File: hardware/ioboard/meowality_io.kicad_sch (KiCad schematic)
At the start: 4 parts

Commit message: Add USB hub and UART ICs
Signed-off-by: gatecat <gatecat@ds0.me>
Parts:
- added C? (x5): 1µ, symbol Device:C_Small
- added C? (x2): 12p, symbol Device:C_Small
- added C? (x3): 10µ, symbol Device:C_Small
- added J? (x2): Conn_01x03, symbol Connector_Generic:Conn_01x03
- added J?: Conn_01x05, symbol Connector_Generic:Conn_01x05
- added R? (x2): 2.2k, symbol Device:R_Small
- added R?: 2.7k, symbol Device:R_Small
- added R? (x4): 1k, symbol Device:R_Small
- added U? (x3): CH330N, Package_SO:SOIC-8_3.9x4.9mm_P1.27mm, symbol Interface_USB:CH330N
- added U?: FE1.1s, Package_SO:SSOP-28_3.9x9.9mm_P0.635mm, symbol Interface_USB:FE1.1s
- added U?: 24LC00, symbol Memory_EEPROM:24LC00
- added Y?: 12MHz, symbol Device:Crystal_GND24
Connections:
- net +3V3: now also U?.3 (VDD), U?.4 (VDD), C?.1, C?.1, C?.1, U?.5 (VCC), U?.5 (VCC), U?.8 (V3), U?.8 (V3)
- net +5V: now also U?.12 (VCONN), U?.13 (VCONN), C?.1, R?.2, U?.20 (VDD5)
- net GND: now also C?.1, C?.1, C?.2, C?.2, C?.2, C?.2, C?.2, C?.2, C?.2, C?.2, J?.3 (Pin_3), J?.3 (Pin_3), J?.5 (Pin_5), R?.1, R?.2, U?.1 (A0), U?.1 (VSS), U?.2 (A1), U?.3 (A2), U?.3 (GND), U?.3 (GND), U?.4 (GND), Y?.2, Y?.4
- net LEFT_UART_RX: now also J?.1 (Pin_1), U?.6 (TXD)
- net LEFT_UART_TX: now also J?.2 (Pin_2), U?.7 (RXD)
- net RIGHT_UART_RX: now also J?.1 (Pin_1), U?.6 (TXD)
- net RIGHT_UART_TX: now also J?.2 (Pin_2), U?.7 (RXD)
- net USB2L_D+: now also U?.7 (DP3)
- net USB2L_D-: now also U?.6 (DM3)
- net USB2R_D+: now also U?.5 (DP4)
- net USB2R_D-: now also U?.4 (DM4)
- net USB2_D+: now also U?.16 (DPU)
- net USB2_D-: now also U?.15 (DMU)
- net VBUS: now also U?.2 (VBUS)
- new net: R?.1, U?.14 (REXT)
- new net: R?.1, U?.18 (VBUSM)
- new net: R?.2, U?.19 (BUSJ)
- new net: C?.2, U?.2 (XOUT), Y?.1
- new net: R?.2, U?.26 (OVCJ)
- new net: C?.2, U?.3 (XIN), Y?.3
- new net HUB_1V8: C?.1, C?.1, U?.12 (VD18_O)
- new net HUB_3V3: C?.1, C?.1, J?.1 (Pin_1), R?.1, R?.1, R?.2, R?.2, U?.13 (VD33), U?.21 (VD33_O), U?.8 (VCC)
- new net HUB_RST: J?.4 (Pin_4), R?.2, U?.17 (~{XRSTJ})
- new net HUB_SCL: J?.3 (Pin_3), R?.1, U?.23 (LED1/EESCL), U?.6 (SCL)
- new net HUB_SDA: J?.2 (Pin_2), R?.1, U?.27 (TESTJ/EESDA), U?.5 (SDA)
- new net USBUART0_D+: U?.1 (UD+), U?.11 (DP1)
- new net USBUART0_D-: U?.10 (DM1), U?.2 (UD-)
- new net USBUART1_D+: U?.1 (UD+), U?.9 (DP2)
- new net USBUART1_D-: U?.2 (UD-), U?.8 (DM2)
- no-connect marks 3 -> 10

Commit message: Add Displayport connector
Signed-off-by: gatecat <gatecat@ds0.me>
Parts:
- removed U?: CH330N, Package_SO:SOIC-8_3.9x4.9mm_P1.27mm, symbol Interface_USB:CH330N
- added F?: 500mA, symbol Device:Polyfuse_Small
- added J?: MINI_DP_SINK, symbol meowality:MINI_DP_SINK
- added R? (x2): 10k, symbol Device:R_Small
- added U? (x2): TPD4E02B04DQA, Package_SON:USON-10_2.5x1.0mm_P0.5mm, symbol Power_Protection:TPD4E02B04DQA
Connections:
- net +3V3: now also F?.1
- net DP_AUX+: now also J?.16 (AUX+)
- net DP_AUX-: now also J?.18 (AUX-)
- net DP_IN_L0+: now also J?.12 (ML_L0+), U?.2 (IO2)
- net DP_IN_L0-: now also J?.10 (ML_L0-), U?.1 (IO1)
- net DP_IN_L1+: now also J?.17 (ML_L1+), U?.5 (IO4)
- net DP_IN_L1-: now also J?.15 (ML_L1-), U?.4 (IO3)
- net DP_IN_L2+: now also J?.11 (ML_L2+), U?.5 (IO4)
- net DP_IN_L2-: now also J?.9 (ML_L2-), U?.4 (IO3)
- net DP_IN_L3+: now also J?.5 (ML_L3+), U?.2 (IO2)
- net DP_IN_L3-: now also J?.3 (ML_L3-), U?.1 (IO1)
- net GND: now also J?.1 (GND), J?.13 (GND), J?.14 (GND), J?.19 (GND), J?.7 (GND), J?.8 (GND), J?.S, R?.2, R?.2, U?.3 (G), U?.3 (G), U?.8 (G), U?.8 (G)
- new net: F?.2, J?.20 (DP_PWR)
- new net: J?.4 (CONFIG1), R?.1
- new net: J?.6 (CONFIG2), R?.1
- new net DP_HPD: J?.2 (HPD)
- no-connect marks 10 -> 9
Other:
- moved on the sheet: C?, J?, R?, U?, Y?

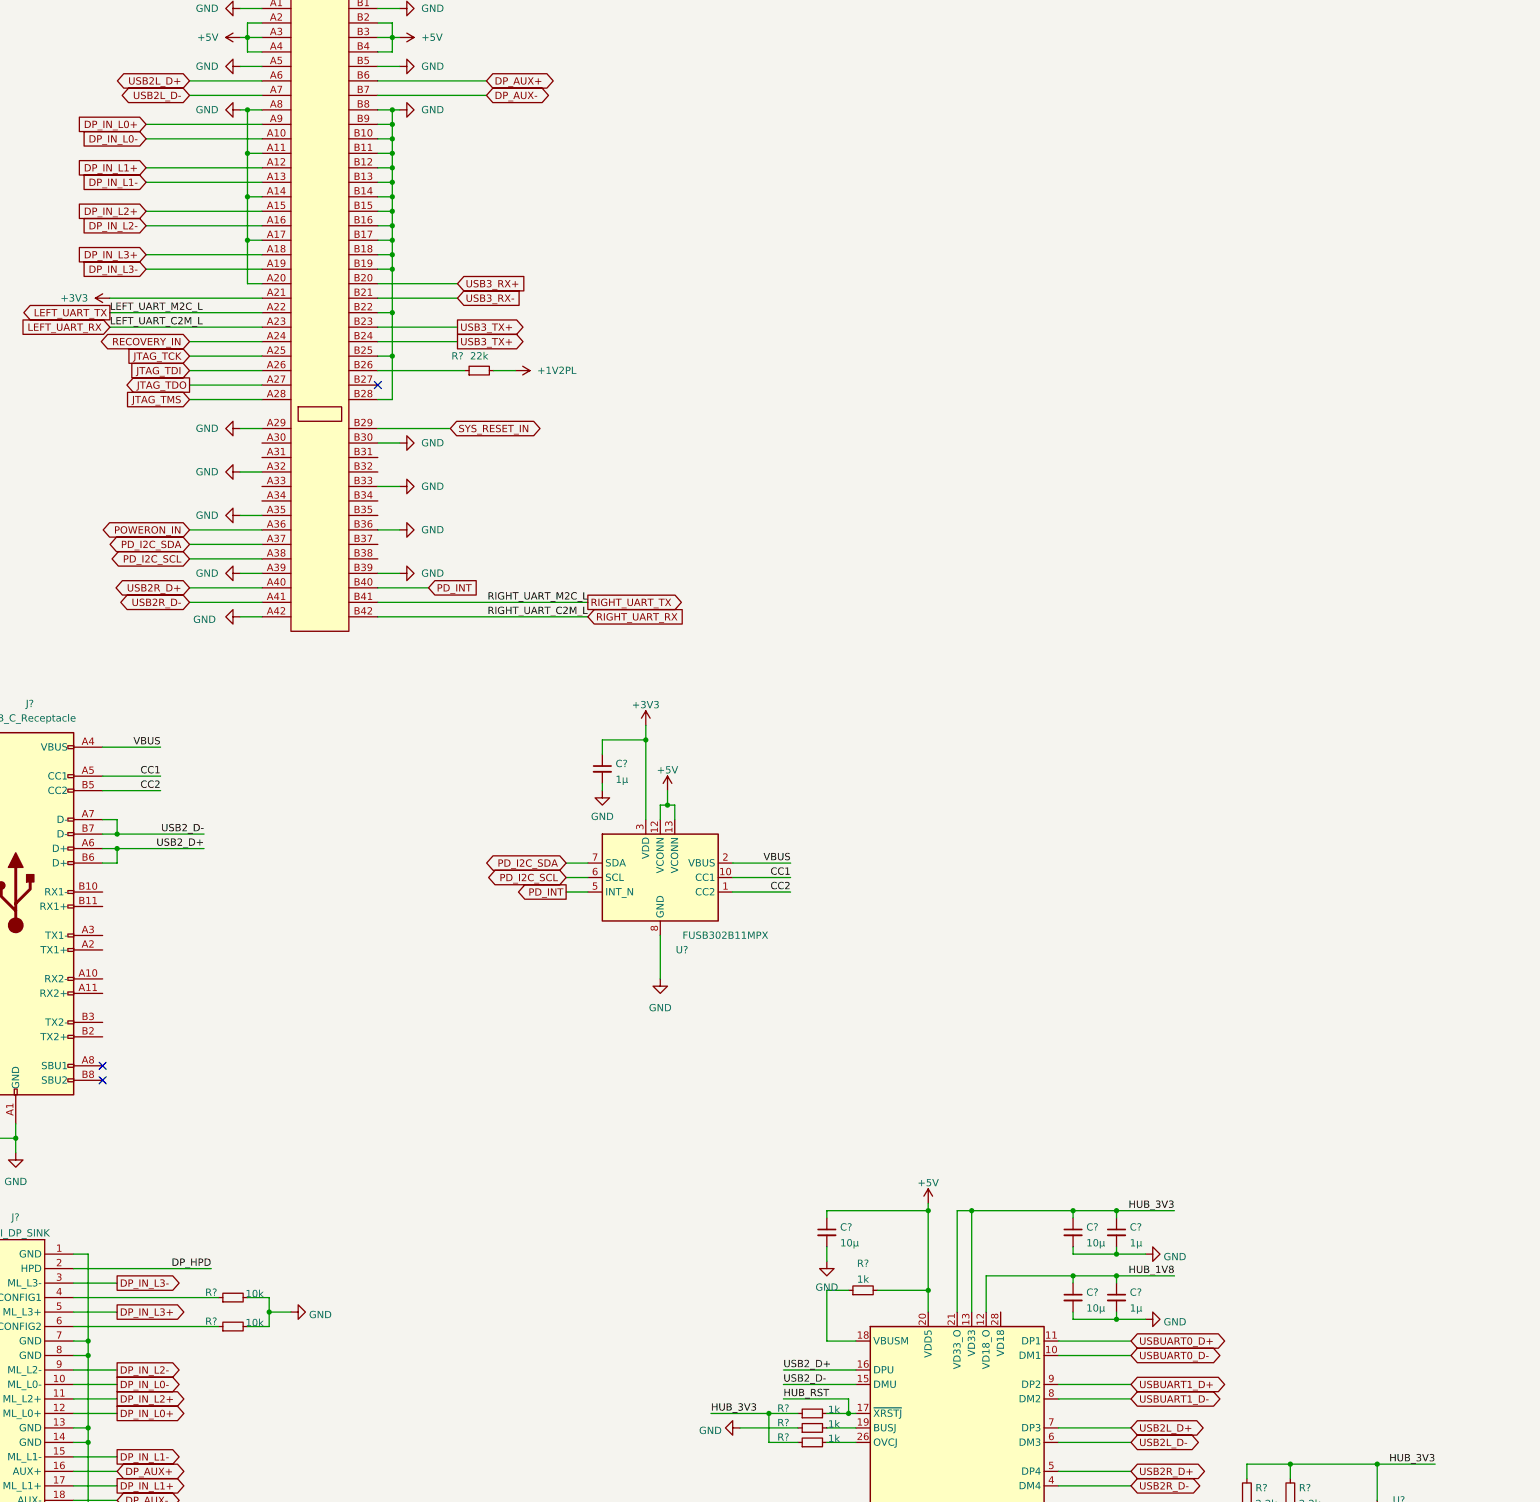
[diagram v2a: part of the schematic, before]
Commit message: Add Vbus to 5V buck
Signed-off-by: gatecat <gatecat@ds0.me>
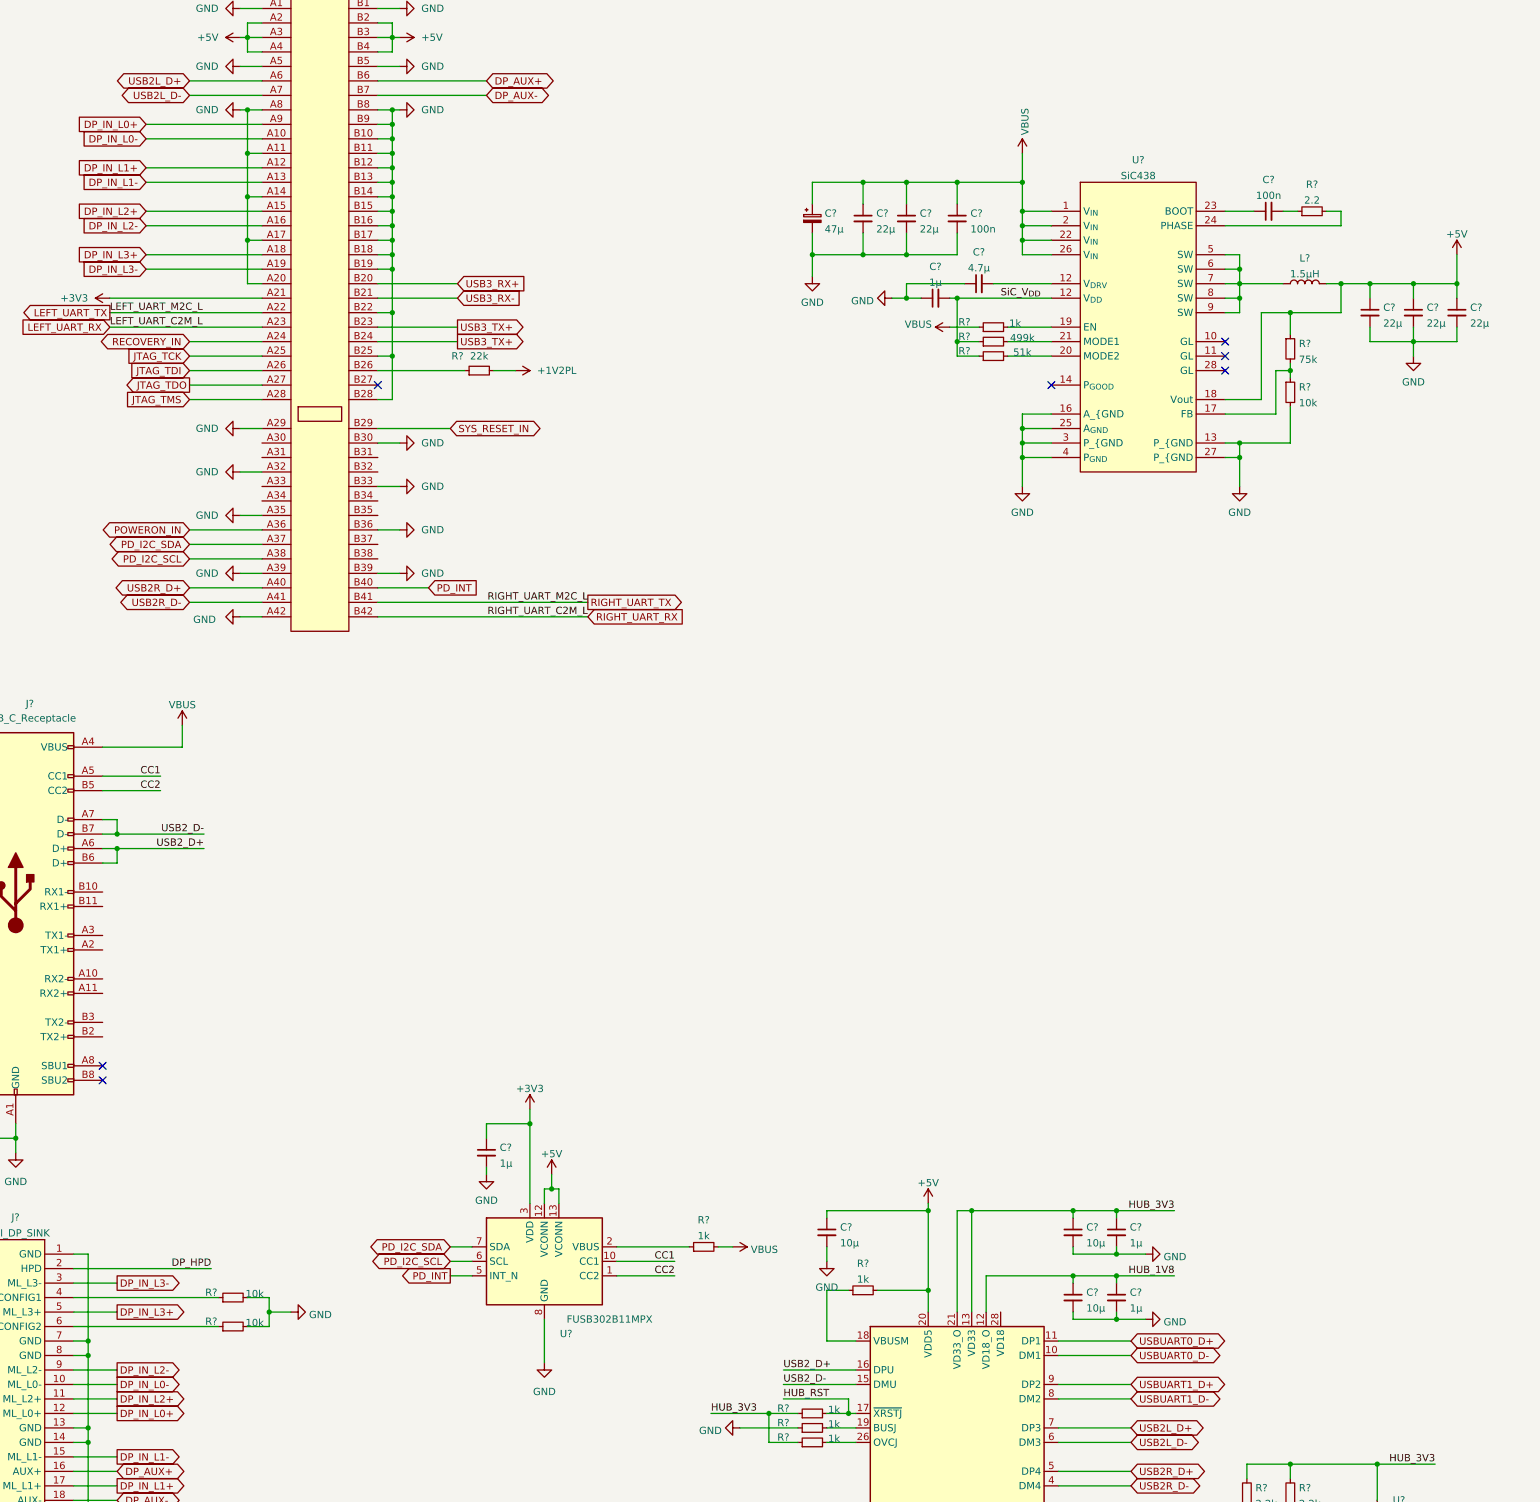
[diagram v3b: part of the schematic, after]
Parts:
- added C? (x5): 22µ, symbol Device:C_Small
- added C?: 47µ, symbol Device:CP_Small
- added C?: 1µ, symbol Device:C_Small
- added C? (x2): 100n, symbol Device:C_Small
- added C?: 4.7µ, symbol Device:C_Small
- added L?: 1.5µH, symbol Device:L
- added R?: 75k, symbol Device:R_Small
- added R?: 499k, symbol Device:R_Small
- added R?: 51k, symbol Device:R_Small
- added R? (x2): 1k, symbol Device:R_Small
- added R?: 10k, symbol Device:R_Small
- added R?: 2.2, symbol Device:R_Small
- added U?: SiC438, symbol meowality:SiC438
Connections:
- net +5V: now also C?.1, C?.1, C?.1, L?.2, R?.1, U?.18 (Vout)
- net GND: now also C?.1, C?.1, C?.2, C?.2, C?.2, C?.2, C?.2, C?.2, C?.2, R?.2, U?.13 (P_{GND), U?.16 (A_{GND), U?.25 (A_{GND}), U?.27 (P_{GND), U?.3 (P_{GND), U?.4 (P_{GND})
- net VBUS: now also C?.1, C?.1, C?.1, C?.1, R?.1, R?.2, U?.1 (V_{IN}), U?.2 (V_{IN}), U?.22 (V_{IN}), U?.26 (V_{IN}); no longer U?.2 (VBUS)
- new net: R?.1, R?.2, U?.17 (FB)
- new net: R?.2, U?.21 (MODE1)
- new net: C?.2, U?.12 (V_{DRV})
- new net: R?.2, U?.19 (EN)
- new net: R?.2, U?.20 (MODE2)
- new net: C?.1, U?.23 (BOOT)
- new net: R?.2, U?.24 (PHASE)
- new net: L?.1, U?.5 (SW), U?.6 (SW), U?.7 (SW), U?.8 (SW), U?.9 (SW)
- new net: C?.2, R?.1
- new net: R?.1, U?.2 (VBUS)
- new net SiC_V_{DD}: C?.2, R?.1, R?.1, U?.12 (V_{DRV})
- no-connect marks 9 -> 13
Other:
- moved on the sheet: C?, U?

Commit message: Add type-C mux; IO exp; 3.3V/1.8V rails
Signed-off-by: gatecat <gatecat@ds0.me>
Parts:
- added C?: 10µ, symbol Device:C_Small
- added C? (x6): 100n, symbol Device:C_Small
- added C? (x4): 1µ, symbol Device:C_Small
- added C? (x2): 22µ, symbol Device:C_Small
- added C?: 10n, symbol Device:C_Small
- added L?: 3.3µ, symbol Device:L_Small
- added R? (x5): 10k, symbol Device:R_Small
- added R? (x2): 100, symbol Device:R_Small
- added R?: 31.6k, symbol Device:R_Small
- added RN? (x2): 1k, symbol Device:R_Pack04
- added SW? (x2): SW_Push, symbol Switch:SW_Push
- added SW?: SW_SPDT, symbol Switch:SW_SPDT
- added U?: PCAL6416APW, Package_SO:TSSOP-24_4.4x7.8mm_P0.65mm, symbol Interface_Expansion:PCAL6416APW
- added U?: LD3985M18R_SOT23, Package_TO_SOT_SMD:SOT-23-5, symbol Regulator_Linear:LD3985M18R_SOT23
- added U?: HDSP-7501, Display_7Segment:HDSP-A151, symbol Display_Character:HDSP-7501
- added U?: CBTL02043A, Package_DFN_QFN:WQFN-20-1EP_2.5x4.5mm_P0.5mm_EP1x2.9mm, symbol Analog_Switch:CBTL02043A
- added U?: AP6230xWU, symbol meowality:AP6230xWU
- C? (x2): value 22µ -> 10µ
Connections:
- net +3V3: now also C?.1, C?.1, C?.1, C?.1, C?.2, L?.2, R?.1, R?.1, R?.1, U?.1 (CA), U?.1 (VDD), U?.1 (VIN), U?.10 (VDD), U?.24 (VDD_P), U?.3 (INH), U?.6 (CA), U?.6 (VDD)
- net +5V: now also C?.1, U?.1 (Vin), U?.5 (EN)
- net DP_HPD: now also U?.5 (P0_1)
- net GND: now also C?.1, C?.1, C?.2, C?.2, C?.2, C?.2, C?.2, C?.2, C?.2, R?.1, R?.2, R?.2, SW?.1, U?.1 (Vin), U?.11 (GND), U?.12 (VSS), U?.2 (GND), U?.20 (GND), U?.21 (GND), U?.5 (GND)
- net PD_I2C_SCL: now also U?.22 (SCL)
- net PD_I2C_SDA: now also U?.23 (SDA)
- net POWERON_IN: now also SW?.2 (B)
- net RECOVERY_IN: now also SW?.1
- net SYS_RESET_IN: now also R?.2, SW?.2
- net USB3_RX+: now also U?.3 (A0_P)
- net USB3_RX-: now also U?.4 (A0_N)
- net USB3_TX+: now also U?.7 (A1_P), U?.8 (A1_N)
- net SSRX2-: now reaches J?.A10 (RX2-)
- net SSRX2-: now also U?.14 (C0_N)
- net SSRX2+: now reaches J?.A11 (RX2+)
- net SSRX2+: now also U?.15 (C0_P)
- net SSTX1+: now reaches J?.A2 (TX1+)
- net SSTX1-: now reaches J?.A3 (TX1-)
- net SSRX1-: now reaches J?.B10 (RX1-)
- net SSRX1-: now also U?.18 (B0_N)
- net SSRX1+: now reaches J?.B11 (RX1+)
- net SSRX1+: now also U?.19 (B0_P)
- net SSTX2+: now reaches J?.B2 (TX2+)
- net SSTX2-: now reaches J?.B3 (TX2-)
- new net: C?.2, L?.1, U?.2 (SW)
- new net: RN?.5 (R4.2), U?.13 (P1_0)
- new net: RN?.6 (R3.2), U?.14 (P1_1)
- new net: RN?.7 (R2.2), U?.15 (P1_2)
- new net: RN?.8 (R1.2), U?.16 (P1_3)
- new net: RN?.5 (R4.2), U?.17 (P1_4)
- new net: RN?.6 (R3.2), U?.18 (P1_5)
- new net: RN?.7 (R2.2), U?.19 (P1_6)
- new net: RN?.8 (R1.2), U?.20 (P1_7)
- new net: R?.2, U?.21 (ADDR)
- new net: R?.2, U?.3 (~{RESET})
- new net: R?.2, SW?.2
- new net: C?.1, U?.4 (BYP)
- new net: RN?.4 (R4.1), U?.10 (A)
- new net: RN?.3 (R3.1), U?.2 (F)
- new net: RN?.2 (R2.1), U?.3 (G)
- new net: RN?.4 (R4.1), U?.4 (E)
- new net: RN?.1 (R1.1), U?.5 (D)
- new net: RN?.1 (R1.1), U?.7 (DP)
- new net: RN?.2 (R2.1), U?.8 (C)
- new net: RN?.3 (R3.1), U?.9 (B)
- new net: R?.2, SW?.1 (A)
- new net: C?.1, U?.6 (BST)
- new net: R?.1, U?.2 (XSD)
- new net: R?.1, R?.2, U?.4 (FB)
- new net +1V8: C?.1, C?.2, R?.1, R?.1, U?.2 (VDD_I2C), U?.5 (VOUT)
- new net SSTXC1+: C?.1, C?.2, U?.17 (B1_P)
- new net SSTXC1-: C?.1, C?.2, U?.16 (B1_N)
- new net SSTXC2+: C?.1, C?.2, U?.13 (C1_P)
- new net SSTXC2-: C?.1, C?.2, U?.12 (C1_N)
- new net USBC_SEL: U?.4 (P0_0), U?.9 (SEL)
- no-connect marks 13 -> 31

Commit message: Fixing various IO board issues
Signed-off-by: gatecat <gatecat@ds0.me>
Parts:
- removed R?: 10k, symbol Device:R_Small
- removed SW?: SW_Push, symbol Switch:SW_Push
- added J6: JTAG, symbol Connector_Generic:Conn_02x07_Odd_Even
- added R21: 100, symbol Device:R_Small
- added SW3: SW_Push, symbol Switch:SW_Push
- gave numbers to parts that had none: 85
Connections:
- net +1V8: now also R21.1
- net +3V3: now also J6.2 (Pin_2)
- net GND: now also J6.1 (Pin_1), J6.11 (Pin_11), J6.13 (Pin_13), J6.3 (Pin_3), J6.5 (Pin_5), J6.7 (Pin_7), J6.9 (Pin_9)
- net HUB_1V8: now also U6.28 (VD18)
- net JTAG_TCK: now also J6.6 (Pin_6)
- net JTAG_TDI: now also J6.10 (Pin_10)
- net JTAG_TDO: now also J6.8 (Pin_8)
- net JTAG_TMS: now also J6.4 (Pin_4)
- net SYS_RESET_IN: now also SW3.1
- new net: R21.2, SW3.2
- no-connect marks 31 -> 33

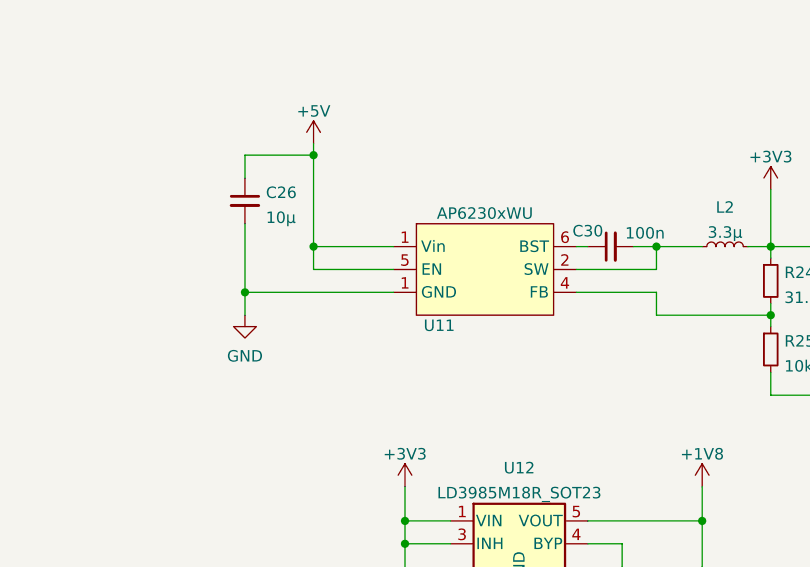
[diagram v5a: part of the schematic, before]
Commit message: Assign most top-board footprints
Signed-off-by: gatecat <gatecat@ds0.me>
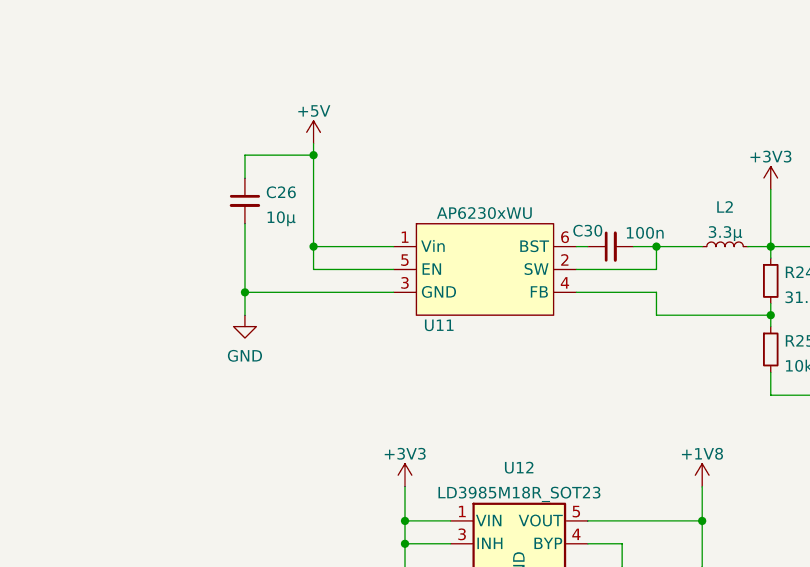
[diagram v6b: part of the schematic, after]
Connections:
- net GND: now also U11.3 (GND); no longer U11.1 (Vin)
